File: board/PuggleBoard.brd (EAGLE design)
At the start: 54.6 x 86.4 mm, 141 parts, among them U1 LMP7704, U10 24C, U2 ADS8331, U3 AD5686, U4 OPA4209, U5 TPS7A3001, U6 TPS7A4901, U7 LTM8045, U8 REF5040, U9 AD8032

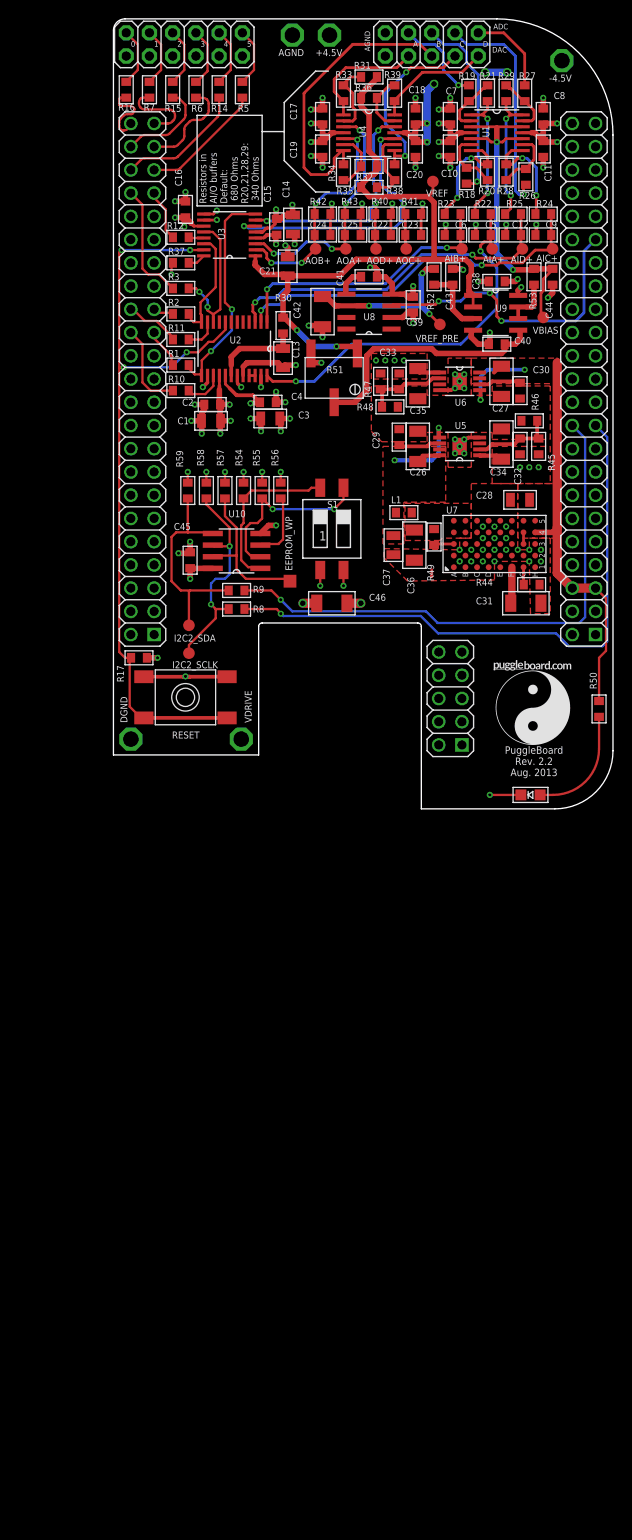
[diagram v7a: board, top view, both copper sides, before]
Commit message: Starting revisions to create r3.0 of the board. Fixed most of the schematic. Added LVDS circuit.
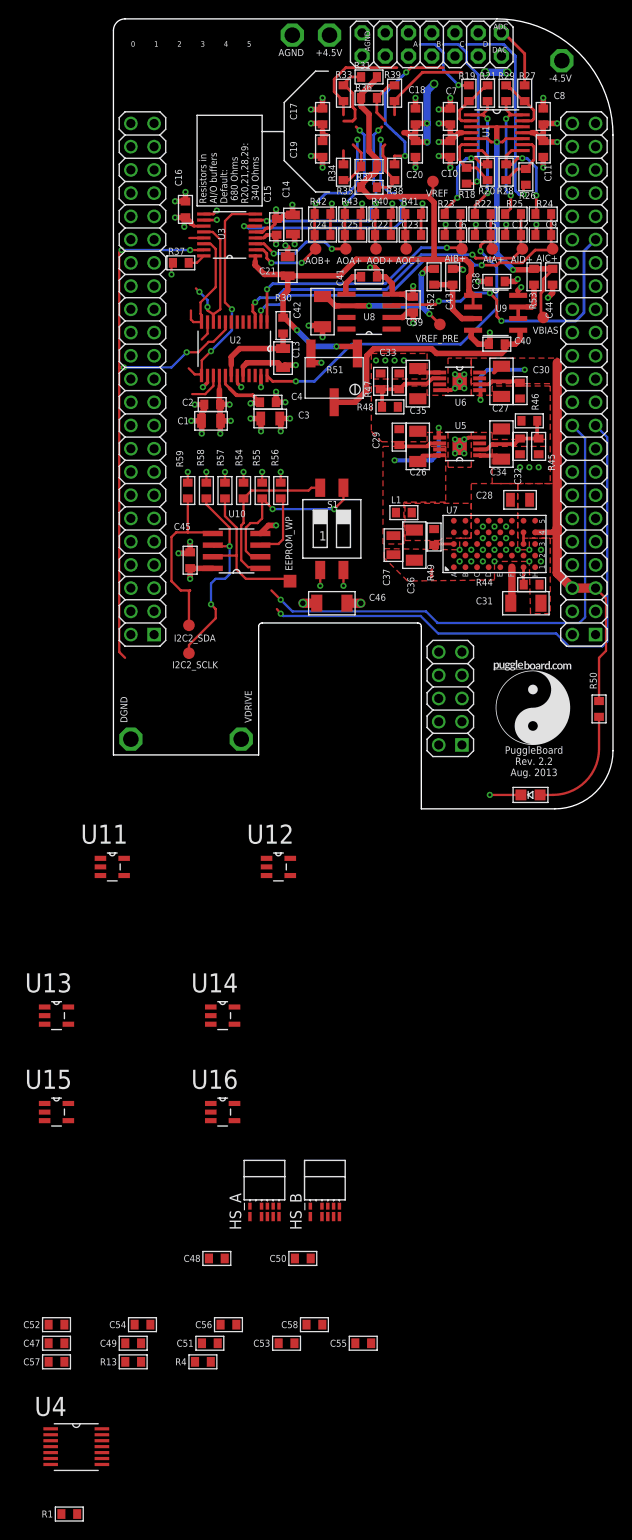
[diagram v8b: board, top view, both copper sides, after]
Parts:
- removed D_I/O: PINHD-2X6, puggleboard:2X06
- removed R10, R11, R12, R14, R15, R16, R2, R3, R5, R6, R7, R8, R9: 33, puggleboard:0603
- removed R17: 10k, puggleboard:0603
- removed RESET: SPST_TACT, puggleboard:EVQ-Q2-A
- added C47, C49, C51, C53, C55, C57: 1nF, puggleboard:0603
- added C48, C50, C52, C54, C56, C58: 0.1uF, puggleboard:0603
- added HS_A, HS_B: RHD2000-CABLE-DAQ-SIDE-SINGLE, puggleboard:OMNETICS_PZN_12_AA-SINGLEBUS
- added R13, R4: 100, puggleboard:0603
- added U11, U12, U13, U15: SN65LVDS1, ti-extended:SOT95P280X145-5N
- added U14, U16: SN65LVDS2, ti-extended:SOT95P280X145-5N
- A_I/O: value PINHD-2X5 -> PINHD-2X7; device puggleboard:2X05 -> puggleboard:2X07
- R1: value 33 -> 10k
- moved U4 147.2 mm to (-4.06, -69.7)
- moved R1 126.2 mm to (-4.83, -77.1)
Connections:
- removed net DIO0: D_I/O.2, R16.1
- removed net DIO1: D_I/O.4, R7.2
- removed net DIO2: D_I/O.6, R15.1
- removed net DIO3: D_I/O.8, R6.2
- removed net DIO4: D_I/O.10, R14.1
- removed net DIO5: D_I/O.12, R5.2
- removed net N$10: BB1.28, R10.2
- removed net N$11: R37.1, U3.16
- removed net N$12: BB1.39, R12.2
- removed net N$15: BB1.42, R14.2
- removed net N$17: BB1.44, R15.2
- removed net N$21: BB1.46, R16.2
- removed net N$23: BB1.45, R7.1
- removed net N$25: BB1.43, R6.1
- removed net N$26: BB1.41, R5.1
- removed net N$3 (its old number): BB1.40, R3.1
- removed net N$31: BB1.65, R8.1
- removed net N$35: BB1.66, R9.2
- removed net N$5: BB1.29, R2.1
- removed net N$7: BB1.27, R1.1
- removed net N$8: BB1.30, R11.2
- new net CS1: U13.5
- new net CS1_N: HS_A.T1, U13.3
- new net CS1_P: HS_A.B1, U13.4
- new net CS2: U15.5
- new net CS2_N: HS_B.T1, U15.3
- new net CS2_P: HS_B.B1, U15.4
- new net EOC: U2.9
- new net MISO1: U14.5
- new net MISO1_N: HS_A.T4, R4.2, U14.3
- new net MISO1_P: HS_A.B4, R4.1, U14.4
- new net MISO2: U16.5
- new net MISO2_N: HS_B.T4, R13.2, U16.3
- new net MISO2_P: HS_B.B4, R13.1, U16.4
- new net MOSI: U12.5
- new net MOSI_N: HS_A.T3, HS_B.T3, U12.3
- new net MOSI_P: HS_A.B3, HS_B.B3, U12.4
- new net SCLK: U11.5
- new net SCLK_N: HS_A.T2, HS_B.T2, U11.3
- new net SCLK_P: HS_A.B2, HS_B.B2, U11.4
- net ADC_A: now also A_I/O.2; no longer A_I/O.4
- net ADC_B: now also A_I/O.4; no longer A_I/O.6
- net ADC_C: now also A_I/O.6; no longer A_I/O.8
- net ADC_D: now also A_I/O.8; no longer A_I/O.10
- net DAC_+IN_A: now also U4.10
- net DAC_+IN_C: no longer U4.10
- net DAC_A: now also A_I/O.10; no longer A_I/O.3
- net DAC_B: now also A_I/O.11; no longer A_I/O.5
- net DAC_C: now also A_I/O.12; no longer A_I/O.7
- net DAC_D: now also A_I/O.13; no longer A_I/O.9
- net GND: now also A_I/O.14, A_I/O.3, A_I/O.5, A_I/O.7, A_I/O.9, C47.2, C48.2, C49.2, C50.2, C51.2, C52.2, C53.2, C54.2, C55.2, C56.2, C57.2, C58.2, HS_A.T6, HS_B.T6, U11.2, U12.2, U13.2, U14.2, U15.2, U16.2; no longer A_I/O.2, D_I/O.11, D_I/O.3, D_I/O.5, D_I/O.7, D_I/O.9, RESET.B, RESET.B'
- net I2C2_SCL: now also BB1.65; no longer R8.2
- net I2C2_SDA: now also BB1.66; no longer R9.1
- net SPI0: no longer R11.1
- net SPI1: no longer R12.1
- net SPI2: no longer R3.2
- net SPI3: no longer R2.2
- net SPI4: no longer R1.2
- net SPI5: no longer R10.1
- net VDRIVE: now also C47.1, C48.1, C49.1, C50.1, C51.1, C52.1, C53.1, C54.1, C55.1, C56.1, C57.1, C58.1, HS_A.B6, HS_B.B6, R1.2, U11.1, U12.1, U13.1, U14.1, U15.1, U16.1; no longer D_I/O.1, R17.2
- net ~RST: now also R1.1, R37.1, U3.16; no longer R17.1, RESET.A, RESET.A'
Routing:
- net N$31: track 65.7 -> 0.00 mm, vias 1 -> 0
- net I2C2_SCL: track 24.1 -> 84.9 mm, vias 2 -> 3
- net N$35: track 60.5 -> 0.00 mm, vias 1 -> 0
- net I2C2_SDA: track 23.8 -> 77.2 mm, vias 0 -> 1
- net DAC_B: track 32.7 -> 1.50 mm
- net ~RST: track 85.3 -> 70.1 mm
- net N$15: track 13.9 -> 0.00 mm
- net N$26: track 13.4 -> 0.00 mm
- net N$3 (its old number): track 13.0 -> 0.00 mm
- net N$25: track 10.8 -> 0.00 mm
- net N$17: track 10.3 -> 0.00 mm
- net GND: track 117.5 -> 107.7 mm, vias 85 -> 84
- net N$10: track 9.68 -> 0.00 mm
- net N$23: track 8.98 -> 0.00 mm
- net N$21: track 8.11 -> 0.00 mm
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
